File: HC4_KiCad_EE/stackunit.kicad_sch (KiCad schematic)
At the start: 18 parts, among them IC11 74HC161, IC12 74HC377

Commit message: 一部を整地
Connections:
- net Level_A0: now also IC12.13 (D4), IC12.2 (Q0); no longer IC11.14 (QA), IC12.3 (D0)
- net Level_A1: now also IC12.14 (D5), IC12.5 (Q1); no longer IC11.13 (QB), IC12.4 (D1)
- net Level_A2: now also IC12.17 (D6), IC12.6 (Q2); no longer IC11.12 (QC), IC12.7 (D2)
- net Level_A3: now also IC12.18 (D7), IC12.9 (Q3); no longer IC11.11 (QD), IC12.8 (D3)
- net Level_B0: now also IC12.19 (Q7); no longer IC12.18 (D7), IC12.2 (Q0)
- net Level_B1: now also IC12.16 (Q6); no longer IC12.17 (D6), IC12.5 (Q1)
- net Level_B2: now also IC12.15 (Q5); no longer IC12.14 (D5), IC12.6 (Q2)
- net Level_B3: now also IC12.12 (Q4); no longer IC12.13 (D4), IC12.9 (Q3)
- net Level_C0: no longer IC12.12 (Q4)
- net Level_C1: no longer IC12.15 (Q5)
- net Level_C2: no longer IC12.16 (Q6)
- net Level_C3: no longer IC12.19 (Q7)
- net Stack_IN0: now also IC12.3 (D0); no longer IC11.3 (A)
- net Stack_IN1: now also IC12.4 (D1); no longer IC11.4 (B)
- net Stack_IN2: now also IC12.7 (D2); no longer IC11.5 (C)
- net Stack_IN3: now also IC12.8 (D3); no longer IC11.6 (D)

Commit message: コミット忘れてたてへ
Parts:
- removed IC11: 74HC161, Package_DIP:DIP-16_W7.62mm_Socket, symbol 74xx_2:74HC161
- removed LD10, LD11, LD8, LD9: LED, LED_THT:LED_Rectangular_W5.0mm_H2.0mm, symbol Device2:LED_
- removed RN3: 1k, Resistor_THT:R_Array_SIP5, symbol Device:R_Network04_Split
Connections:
- no-connect marks 1 -> 0
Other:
- moved on the sheet: IC12

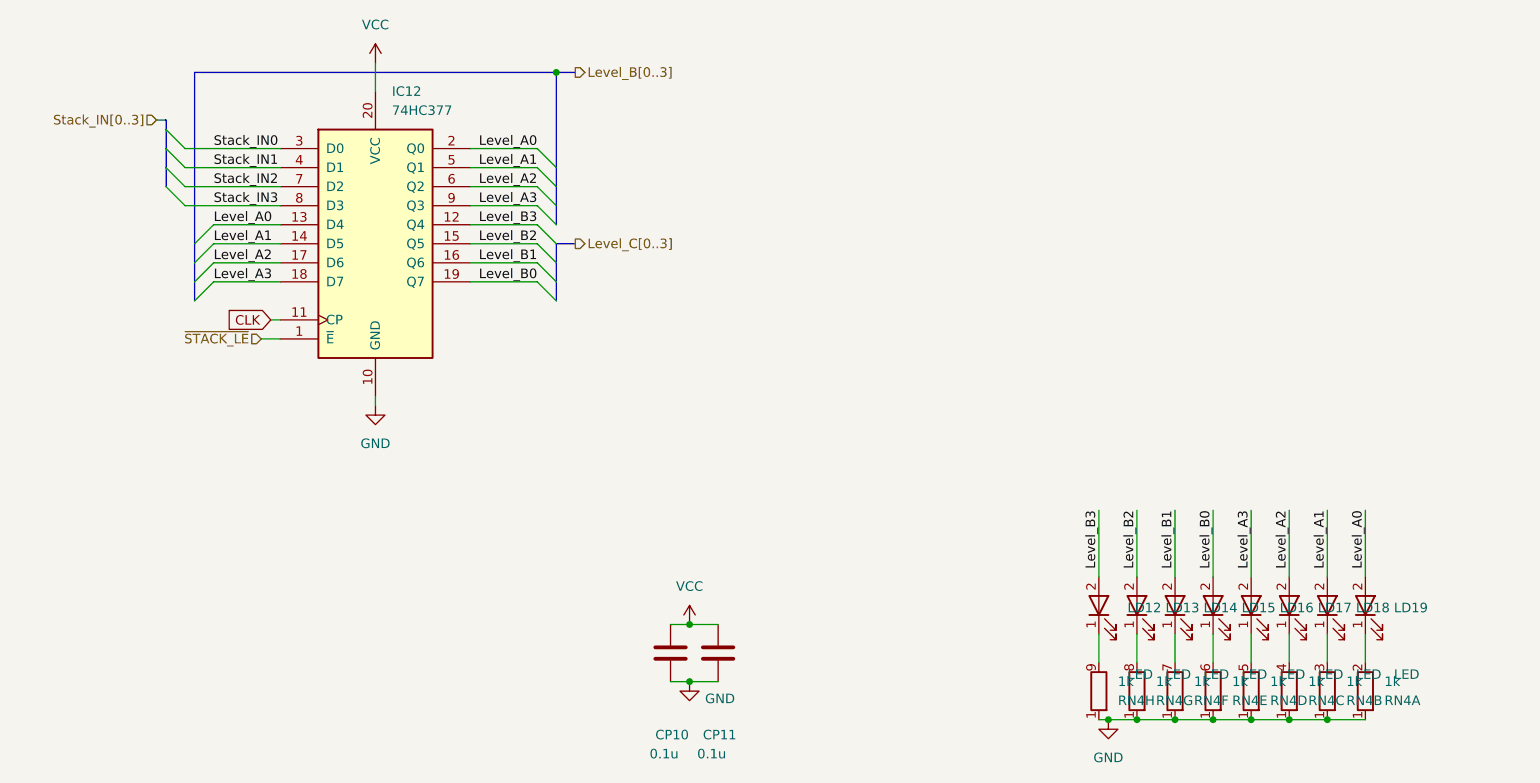
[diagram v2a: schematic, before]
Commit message: 4809を別シートに、ほか
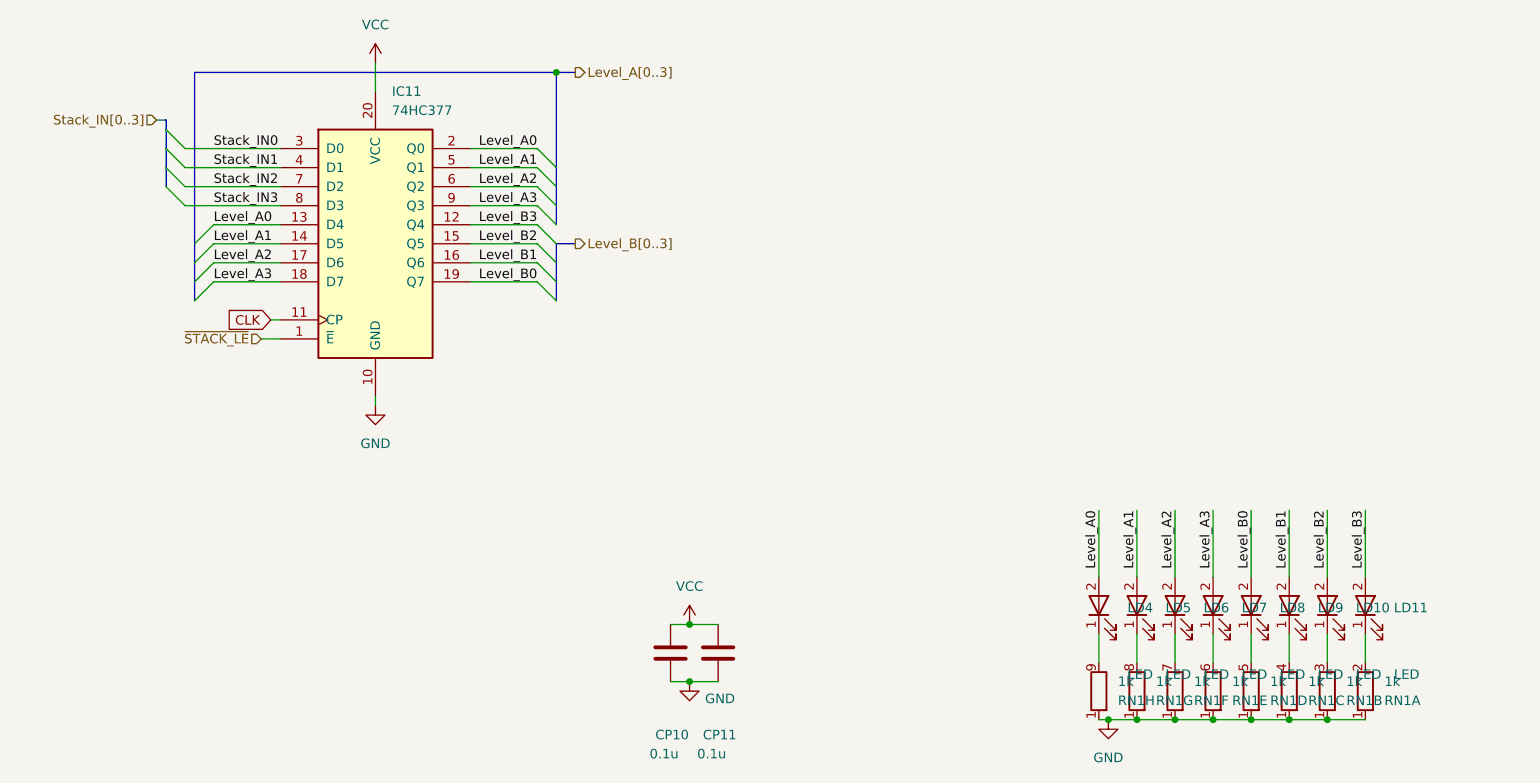
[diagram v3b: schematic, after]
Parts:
- renumbered IC12 to IC11, LD18 to LD10, LD19 to LD11, LD12 to LD4, LD13 to LD5, LD14 to LD6, LD15 to LD7, LD16 to LD8, LD17 to LD9, RN4 to RN1
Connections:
- net Level_A0: now also LD4.2; no longer LD11.2
- net Level_A1: now also LD5.2; no longer LD10.2
- net Level_A2: now also LD6.2; no longer LD9.2
- net Level_A3: now also LD7.2; no longer LD8.2
- net Level_B0: now also LD8.2; no longer LD7.2
- net Level_B1: now also LD9.2; no longer LD6.2
- net Level_B2: now also LD10.2; no longer LD5.2
- net Level_B3: now also LD11.2; no longer LD4.2

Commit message: 完成かも～
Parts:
- removed CP11: 0.1u, Capacitor_THT:C_Disc_D3.0mm_W1.6mm_P2.50mm, symbol Device2:C_Bypass
- renumbered IC11 to IC8, LD4 to LD15, LD5 to LD16, LD6 to LD17, LD7 to LD18, LD8 to LD19, LD9 to LD20, LD10 to LD21, LD11 to LD22, RN1 to RN5
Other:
- moved on the sheet: CP10

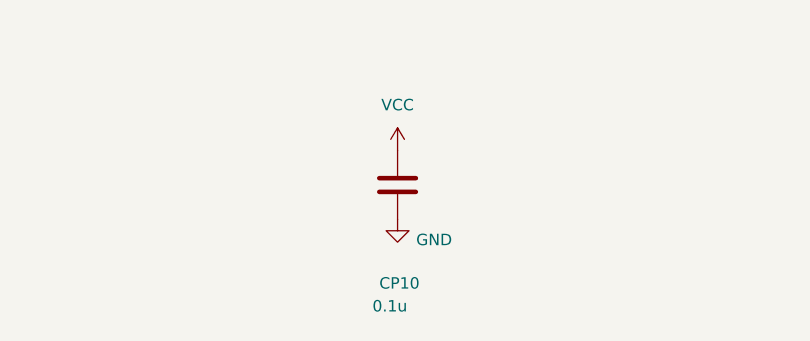
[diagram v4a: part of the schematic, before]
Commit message: Carry_ENを論理反転、回路図の修正
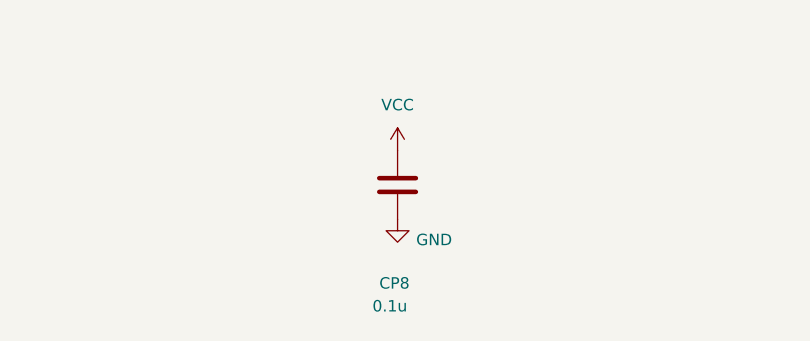
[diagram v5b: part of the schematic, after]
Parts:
- renumbered CP10 to CP8
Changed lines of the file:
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@@
 		(on_board yes)
 		(dnp no)
-		(property "Reference" "CP10"
+		(property "Reference" "CP8"
 			(at 98.298 160.782 0)
 			(effects
@@
 			(project "HC4_KiCad"
 				(path "/33731ded-38c0-4297-bdd8-92b082f46ff8/27e10803-908c-4418-a733-f902d25b5ad6"
-					(reference "CP10")
+					(reference "CP8")
 					(unit 1)
 				)

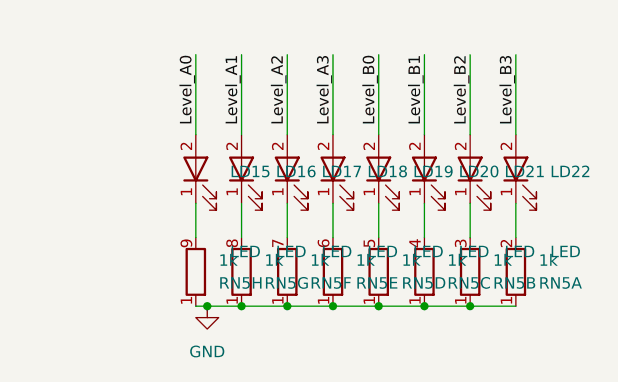
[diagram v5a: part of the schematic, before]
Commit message: PortBを4511に、フットプリントの割り付け開始
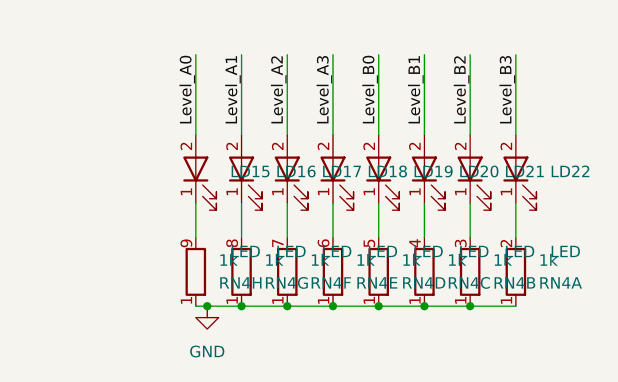
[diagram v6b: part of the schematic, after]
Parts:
- CP8: footprint Capacitor_THT:C_Disc_D3.0mm_W1.6mm_P2.50mm -> Capacitor_SMD:C_0603_1608Metric
- IC8: footprint Package_DIP:DIP-20_W7.62mm_Socket -> Package_SO:SOP-20_7.5x12.8mm_P1.27mm
- renumbered RN5 to RN4
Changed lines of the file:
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@@
 		(dnp no)
 		(fields_autoplaced yes)
-		(property "Reference" "RN5"
+		(property "Reference" "RN4"
 			(at 193.04 156.2101 0)
 			(effects
@@
 			(project ""
 				(path "/33731ded-38c0-4297-bdd8-92b082f46ff8/27e10803-908c-4418-a733-f902d25b5ad6"
-					(reference "RN5")
+					(reference "RN4")
 					(unit 1)
 				)
@@
 		(dnp no)
 		(fields_autoplaced yes)
-		(property "Reference" "RN5"
+		(property "Reference" "RN4"
 			(at 187.96 156.2101 0)
 			(effects
@@
 			(project ""
 				(path "/33731ded-38c0-4297-bdd8-92b082f46ff8/27e10803-908c-4418-a733-f902d25b5ad6"
-					(reference "RN5")
+					(reference "RN4")
 					(unit 2)
 				)
@@
 		(dnp no)
 		(fields_autoplaced yes)
-		(property "Reference" "RN5"
+		(property "Reference" "RN4"
 			(at 157.48 156.2101 0)
 			(effects
@@
 			(project ""
 				(path "/33731ded-38c0-4297-bdd8-92b082f46ff8/27e10803-908c-4418-a733-f902d25b5ad6"
-					(reference "RN5")
+					(reference "RN4")
 					(unit 8)
 				)
@@
 		(on_board yes)
 		(dnp no)
-		(property "Reference" "#PWR029"
+		(property "Reference" "#PWR031"
 			(at 58.42 74.93 0)
 			(effects
@@
 			(project ""
 				(path "/33731ded-38c0-4297-bdd8-92b082f46ff8/27e10803-908c-4418-a733-f902d25b5ad6"
-					(reference "#PWR029")
+					(reference "#PWR031")
 					(unit 1)
 				)
@@
 			)
 		)
-		(property "Footprint" "Package_DIP:DIP-20_W7.62mm_Socket"
+		(property "Footprint" "Package_SO:SOP-20_7.5x12.8mm_P1.27mm"
 			(at 58.42 95.25 0)
 			(effects
@@
 		(dnp no)
 		(fields_autoplaced yes)
-		(property "Reference" "#PWR031"
+		(property "Reference" "#PWR033"
 			(at 100.33 149.86 0)
 			(effects
@@
 			(project ""
 				(path "/33731ded-38c0-4297-bdd8-92b082f46ff8/27e10803-908c-4418-a733-f902d25b5ad6"
-					(reference "#PWR031")
+					(reference "#PWR033")
 					(unit 1)
 				)
@@
 		(on_board yes)
 		(dnp no)
-		(property "Reference" "#PWR032"
+		(property "Reference" "#PWR034"
 			(at 100.33 160.02 0)
 			(effects
@@
 			(project ""
 				(path "/33731ded-38c0-4297-bdd8-92b082f46ff8/27e10803-908c-4418-a733-f902d25b5ad6"
-					(reference "#PWR032")
+					(reference "#PWR034")
 					(unit 1)
 				)
@@
 			)
 		)
-		(property "Footprint" "Capacitor_THT:C_Disc_D3.0mm_W1.6mm_P2.50mm"
+		(property "Footprint" "Capacitor_SMD:C_0603_1608Metric"
 			(at 101.2952 153.67 0)
 			(effects
@@
 		(dnp no)
 		(fields_autoplaced yes)
-		(property "Reference" "#PWR033"
+		(property "Reference" "#PWR035"
 			(at 156.21 165.1 0)
 			(effects
@@
 			(project ""
 				(path "/33731ded-38c0-4297-bdd8-92b082f46ff8/27e10803-908c-4418-a733-f902d25b5ad6"
-					(reference "#PWR033")
+					(reference "#PWR035")
 					(unit 1)
 				)
@@
 		(dnp no)
 		(fields_autoplaced yes)
-		(property "Reference" "#PWR030"
+		(property "Reference" "#PWR032"
 			(at 58.42 123.19 0)
 			(effects
@@
 			(project ""
 				(path "/33731ded-38c0-4297-bdd8-92b082f46ff8/27e10803-908c-4418-a733-f902d25b5ad6"
-					(reference "#PWR030")
+					(reference "#PWR032")
 					(unit 1)
 				)
@@
 		(dnp no)
 		(fields_autoplaced yes)
-		(property "Reference" "RN5"
+		(property "Reference" "RN4"
 			(at 162.56 156.2101 0)
 			(effects
@@
 			(project ""
 				(path "/33731ded-38c0-4297-bdd8-92b082f46ff8/27e10803-908c-4418-a733-f902d25b5ad6"
-					(reference "RN5")
+					(reference "RN4")
 					(unit 7)
 				)
@@
 		(dnp no)
 		(fields_autoplaced yes)
-		(property "Reference" "RN5"
+		(property "Reference" "RN4"
 			(at 182.88 156.2101 0)
 			(effects
@@
 			(project ""
 				(path "/33731ded-38c0-4297-bdd8-92b082f46ff8/27e10803-908c-4418-a733-f902d25b5ad6"
-					(reference "RN5")
+					(reference "RN4")
 					(unit 3)
 				)
@@
 		(dnp no)
 		(fields_autoplaced yes)
-		(property "Reference" "RN5"
+		(property "Reference" "RN4"
 			(at 172.72 156.2101 0)
 			(effects
@@
 			(project ""
 				(path "/33731ded-38c0-4297-bdd8-92b082f46ff8/27e10803-908c-4418-a733-f902d25b5ad6"
-					(reference "RN5")
+					(reference "RN4")
 					(unit 5)
 				)
@@
 		(dnp no)
 		(fields_autoplaced yes)
-		(property "Reference" "RN5"
+		(property "Reference" "RN4"
 			(at 177.8 156.2101 0)
 			(effects
@@
 			(project ""
 				(path "/33731ded-38c0-4297-bdd8-92b082f46ff8/27e10803-908c-4418-a733-f902d25b5ad6"
-					(reference "RN5")
+					(reference "RN4")
 					(unit 4)
 				)
@@
 		(dnp no)
 		(fields_autoplaced yes)
-		(property "Reference" "RN5"
+		(property "Reference" "RN4"
 			(at 167.64 156.2101 0)
 			(effects
@@
 			(project ""
 				(path "/33731ded-38c0-4297-bdd8-92b082f46ff8/27e10803-908c-4418-a733-f902d25b5ad6"
-					(reference "RN5")
+					(reference "RN4")
 					(unit 6)
 				)

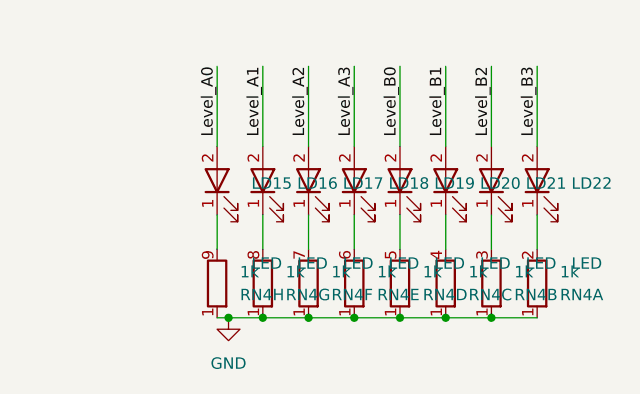
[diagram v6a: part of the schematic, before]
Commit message: チップ集合抵抗に変更、基板作成開始
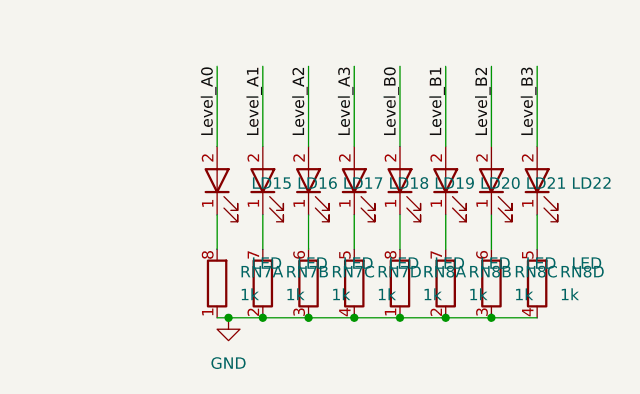
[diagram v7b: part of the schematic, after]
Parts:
- removed RN4: 1k, Resistor_THT:R_Array_SIP9, symbol Device:R_Network08_Split
- added RN7, RN8: 1k, Resistor_SMD:R_Array_Convex_4x0603, symbol Device:R_Pack04_Split
- IC8: footprint Package_SO:SOP-20_7.5x12.8mm_P1.27mm -> Package_SO:TSSOP-20_4.4x6.5mm_P0.65mm
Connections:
- net GND: now also RN7.1 (R1.1), RN7.2 (R2.1), RN7.3 (R3.1), RN7.4 (R4.1), RN8.1 (R1.1), RN8.2 (R2.1), RN8.3 (R3.1), RN8.4 (R4.1)
- net at LD22.1 (K): now also RN8.5 (R4.2)
- net at LD21.1 (K): now also RN8.6 (R3.2)
- net at LD15.1 (K): now also RN7.8 (R1.2)
- net at LD20.1 (K): now also RN8.7 (R2.2)
- net at LD18.1 (K): now also RN7.5 (R4.2)
- net at LD19.1 (K): now also RN8.8 (R1.2)
- net at LD17.1 (K): now also RN7.6 (R3.2)
- net at LD16.1 (K): now also RN7.7 (R2.2)

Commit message: 配線進捗、7474を使った変な回路
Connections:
- net at RN8.5 (R4.2): now also LD19.1 (K); no longer LD22.1 (K)
- net at LD20.1 (K): now also RN8.6 (R3.2); no longer RN8.7 (R2.2)
- net at RN8.8 (R1.2): now also LD22.1 (K); no longer LD19.1 (K)
- net at LD21.1 (K): now also RN8.7 (R2.2); no longer RN8.6 (R3.2)
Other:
- moved on the sheet: RN8A, RN8B, RN8C, RN8D
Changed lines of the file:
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@@
+	)
+	(junction
+		(at 156.21 158.75)
+		(diameter 0)
+		(color 0 0 0 0)
+	)
+	(junction
+		(at 185.42 158.75)
+		(diameter 0)
+		(color 0 0 0 0)
 	)
 	(junction
@@
 	)
 	(junction
-		(at 156.21 158.75)
-		(diameter 0)
-		(color 0 0 0 0)
-	)
-	(junction
 		(at 170.18 158.75)
-		(diameter 0)
-		(color 0 0 0 0)
-	)
-	(junction
-		(at 185.42 158.75)
 		(diameter 0)
 		(color 0 0 0 0)
@@
 	(wire
 		(pts
+			(xy 185.42 158.75) (xy 190.5 158.75)
+		)
+		(stroke
+			(width 0)
+			(type default)
+		)
+	)
+	(wire
+		(pts
 			(xy 45.72 97.79) (xy 36.83 97.79)
 		)
@@
 	(wire
 		(pts
+			(xy 180.34 158.75) (xy 185.42 158.75)
+		)
+		(stroke
+			(width 0)
+			(type default)
+		)
+	)
+	(wire
+		(pts
 			(xy 175.26 147.32) (xy 175.26 151.13)
 		)
@@
 	(wire
 		(pts
+			(xy 175.26 158.75) (xy 180.34 158.75)
+		)
+		(stroke
+			(width 0)
+			(type default)
+		)
+	)
+	(wire
+		(pts
 			(xy 80.01 97.79) (xy 71.12 97.79)
 		)
@@
 		)
 	)
-	(wire
-		(pts
-			(xy 180.34 158.75) (xy 185.42 158.75)
-		)
-		(stroke
-			(width 0)
-			(type default)
-		)
-	)
 	(bus
 		(pts
@@
 	(wire
 		(pts
-			(xy 175.26 158.75) (xy 180.34 158.75)
-		)
-		(stroke
-			(width 0)
-			(type default)
-		)
-	)
-	(wire
-		(pts
 			(xy 71.12 90.17) (xy 80.01 90.17)
 		)
@@
 		(pts
 			(xy 34.29 95.25) (xy 34.29 72.39)
-		)
-		(stroke
-			(width 0)
-			(type default)
-		)
-	)
-	(wire
-		(pts
-			(xy 185.42 158.75) (xy 190.5 158.75)
 		)
 		(stroke
@@
 	(symbol
 		(lib_id "Device:R_Pack04_Split")
-		(at 190.5 154.94 0)
+		(at 175.26 154.94 0)
 		(unit 4)
 		(exclude_from_sim no)
@@
 		(on_board yes)
 		(dnp no)
-		(fields_autoplaced yes)
 		(property "Reference" "RN8"
-			(at 193.04 153.6699 0)
+			(at 177.8 153.6699 0)
 			(effects
 				(font
@@
 		)
 		(property "Value" "1k"
-			(at 193.04 156.2099 0)
+			(at 177.8 156.2099 0)
 			(effects
 				(font
@@
 		)
 		(property "Footprint" "Resistor_SMD:R_Array_Convex_4x0603"
-			(at 188.468 154.94 90)
+			(at 173.228 154.94 90)
 			(effects
 				(font
@@
 		)
 		(property "Datasheet" "~"
-			(at 190.5 154.94 0)
+			(at 175.26 154.94 0)
 			(effects
 				(font
@@
 		)
 		(property "Description" "4 resistor network, parallel topology, split"
-			(at 190.5 154.94 0)
+			(at 175.26 154.94 0)
 			(effects
 				(font
@@
 	(symbol
 		(lib_id "Device:R_Pack04_Split")
-		(at 175.26 154.94 0)
+		(at 190.5 154.94 0)
 		(unit 1)
 		(exclude_from_sim no)
@@
 		(on_board yes)
 		(dnp no)
-		(fields_autoplaced yes)
 		(property "Reference" "RN8"
-			(at 177.8 153.6699 0)
+			(at 193.04 153.6699 0)
 			(effects
 				(font
@@
 		)
 		(property "Value" "1k"
-			(at 177.8 156.2099 0)
+			(at 193.04 156.2099 0)
 			(effects
 				(font
@@
 		)
 		(property "Footprint" "Resistor_SMD:R_Array_Convex_4x0603"
-			(at 173.228 154.94 90)
+			(at 188.468 154.94 90)
 			(effects
 				(font
@@
 		)
 		(property "Datasheet" "~"
-			(at 175.26 154.94 0)
+			(at 190.5 154.94 0)
 			(effects
 				(font
@@
 		)
 		(property "Description" "4 resistor network, parallel topology, split"
-			(at 175.26 154.94 0)
+			(at 190.5 154.94 0)
 			(effects
 				(font
@@
 	(symbol
 		(lib_id "Device:R_Pack04_Split")
-		(at 180.34 154.94 0)
+		(at 185.42 154.94 0)
 		(unit 2)
 		(exclude_from_sim no)
@@
 		(on_board yes)
 		(dnp no)
-		(fields_autoplaced yes)
 		(property "Reference" "RN8"
-			(at 182.88 153.6699 0)
+			(at 187.96 153.6699 0)
 			(effects
 				(font
@@
 		)
 		(property "Value" "1k"
-			(at 182.88 156.2099 0)
+			(at 187.96 156.2099 0)
 			(effects
 				(font
@@
 		)
 		(property "Footprint" "Resistor_SMD:R_Array_Convex_4x0603"
-			(at 178.308 154.94 90)
+			(at 183.388 154.94 90)
 			(effects
 				(font
@@
 		)
 		(property "Datasheet" "~"
-			(at 180.34 154.94 0)
+			(at 185.42 154.94 0)
 			(effects
 				(font
@@
 		)
 		(property "Description" "4 resistor network, parallel topology, split"
-			(at 180.34 154.94 0)
+			(at 185.42 154.94 0)
 			(effects
 				(font
@@
 	(symbol
 		(lib_id "Device:R_Pack04_Split")
-		(at 185.42 154.94 0)
+		(at 180.34 154.94 0)
 		(unit 3)
 		(exclude_from_sim no)
@@
 		(on_board yes)
 		(dnp no)
-		(fields_autoplaced yes)
 		(property "Reference" "RN8"
-			(at 187.96 153.6699 0)
+			(at 182.88 153.6699 0)
 			(effects
 				(font
@@
 		)
 		(property "Value" "1k"
-			(at 187.96 156.2099 0)
+			(at 182.88 156.2099 0)
 			(effects
 				(font
@@
 		)
 		(property "Footprint" "Resistor_SMD:R_Array_Convex_4x0603"
-			(at 183.388 154.94 90)
+			(at 178.308 154.94 90)
 			(effects
 				(font
@@
 		)
 		(property "Datasheet" "~"
-			(at 185.42 154.94 0)
+			(at 180.34 154.94 0)
 			(effects
 				(font
@@
 		)
 		(property "Description" "4 resistor network, parallel topology, split"
-			(at 185.42 154.94 0)
-			(effects
-				(font
+			(at 180.34 154.94 0)
+			(effects
+				(font
